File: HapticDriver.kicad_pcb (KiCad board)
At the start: 4 copper layers, 54.1 x 29 mm, 56 parts, among them J1 Conn_01x02_Pin, J10 Conn_01x02_Pin, J11 Conn_01x02_Pin, J12 Conn_01x02_Pin, J13 Conn_01x02_Pin, J14 USB_C_Receptacle_USB2.0, J2 Conn_01x02_Pin, J3 BATT PWR, J4 Conn_01x02_Pin, J5 Conn_01x02_Pin, J6 Conn_01x02_Pin, J7 Conn_01x02_Pin, J8 Conn_01x02_Pin, J9 Conn_01x02_Pin, SW1 BOOT, SW2 EN, U1 ESP32-S3-WROOM-2, U10 DRV8847SPWR, U11 REG1117-3.3, U2 DRV8847SPWR, U3 74HCT595, U4 74HCT595, U5 74HCT595, U6 DRV8847SPWR, U7 DRV8847SPWR, U8 DRV8847SPWR, U9 DRV8847SPWR

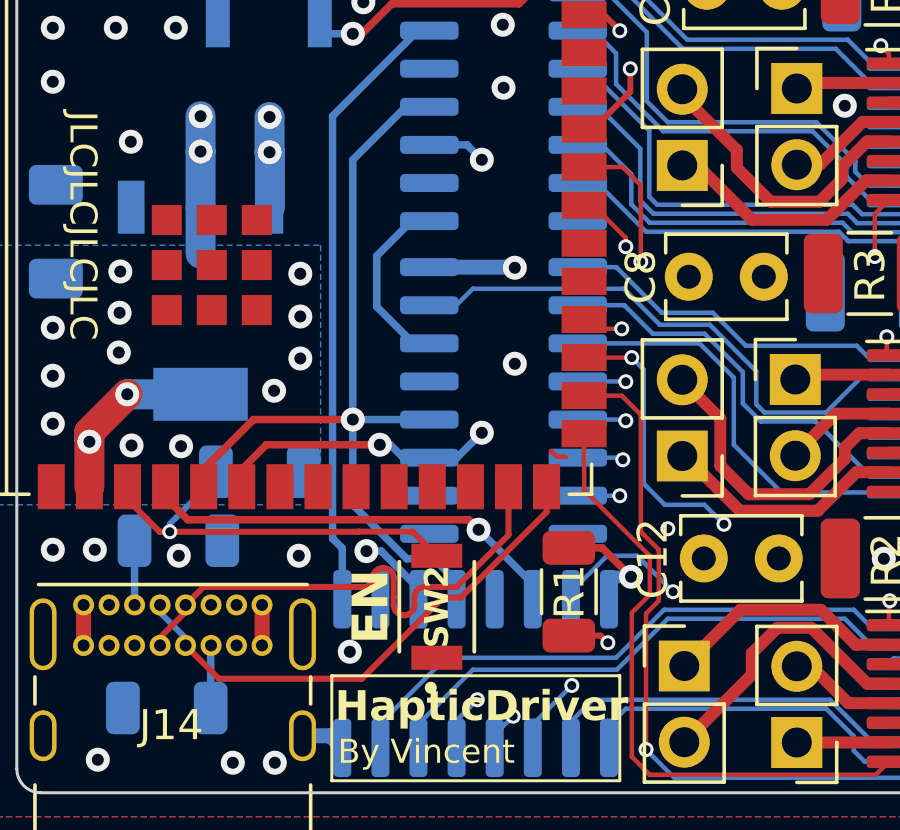
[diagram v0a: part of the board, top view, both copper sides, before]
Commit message: feat: pull OE and CLR shift reg pins to correct voltages
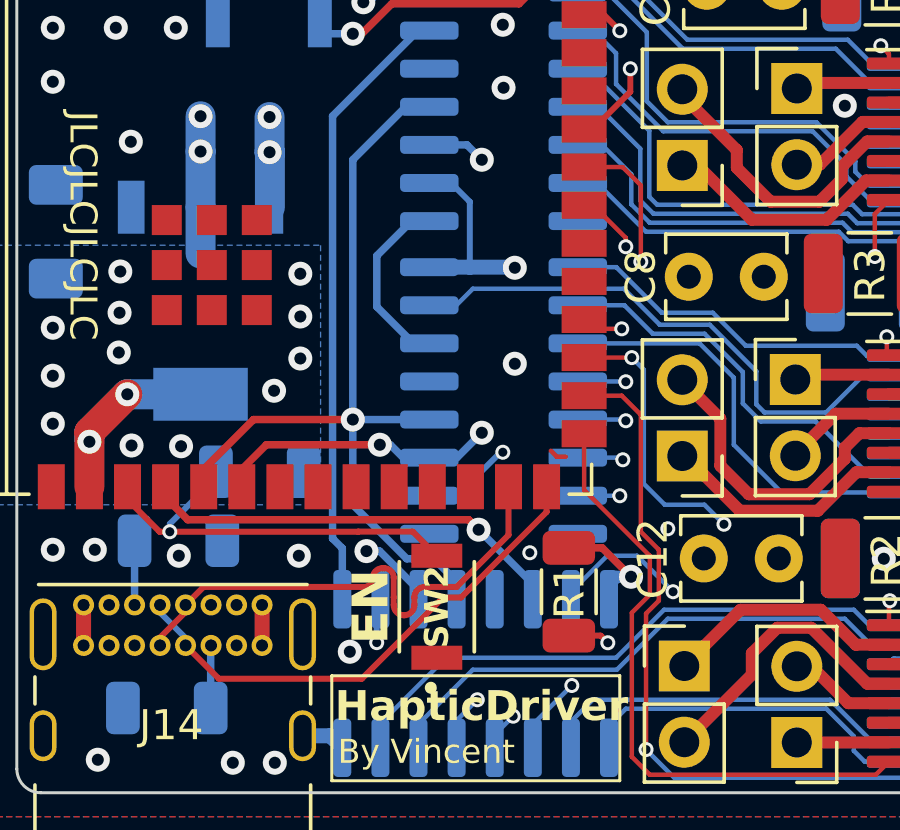
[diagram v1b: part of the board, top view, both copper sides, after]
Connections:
- U3 pad 10: unconnected-(U3-~{SRCLR}-Pad10) -> +3V3
- U3 pad 13: unconnected-(U3-~{OE}-Pad13) -> GND
- U4 pad 10: unconnected-(U4-~{SRCLR}-Pad10) -> +3V3
- U4 pad 13: unconnected-(U4-~{OE}-Pad13) -> GND
- U5 pad 10: unconnected-(U5-~{SRCLR}-Pad10) -> +3V3
- U5 pad 13: unconnected-(U5-~{OE}-Pad13) -> GND
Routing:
- net +3V3: track 72.2 -> 80.5 mm, vias 25 -> 27
- net GND: vias 34 -> 35

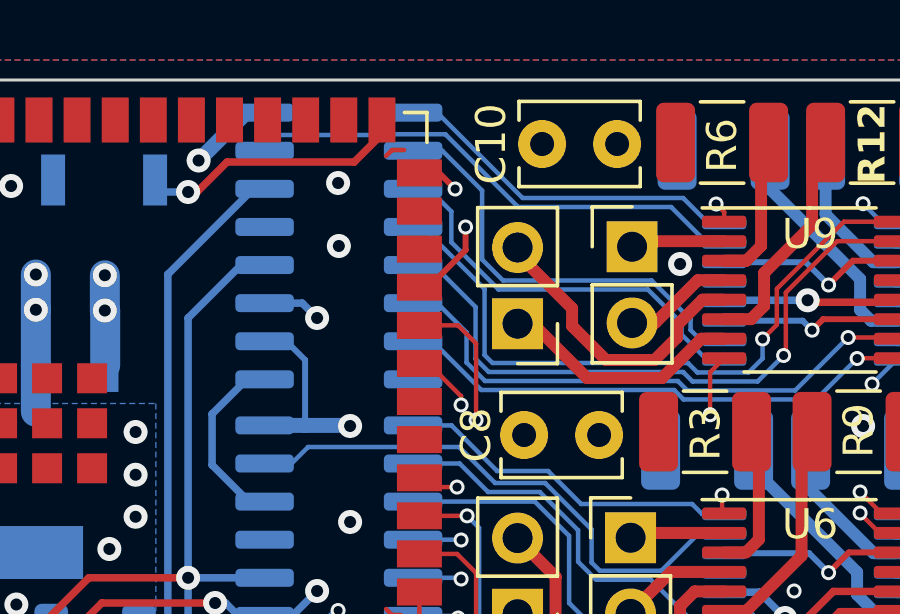
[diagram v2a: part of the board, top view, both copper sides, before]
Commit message: fix: avoid SDA on strapping pin GPIO45
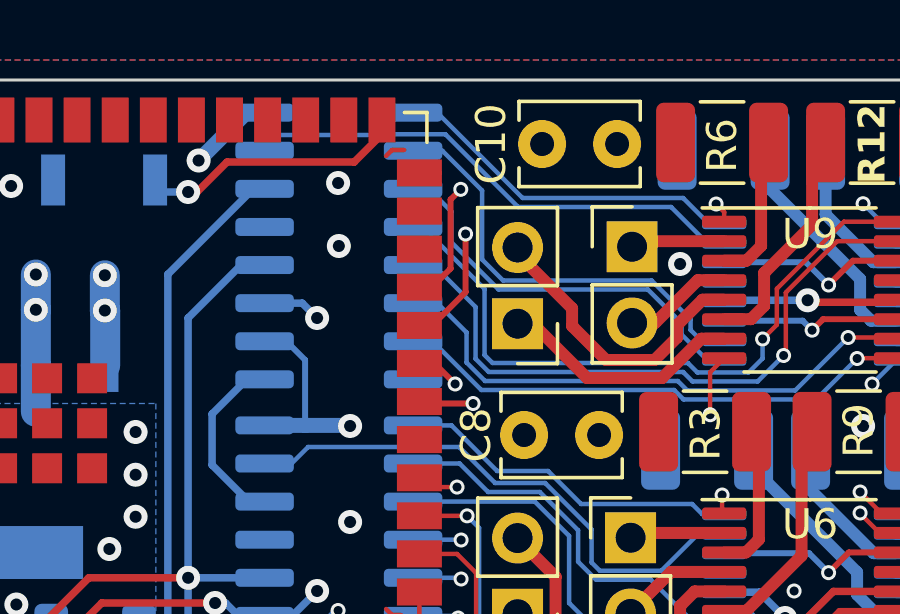
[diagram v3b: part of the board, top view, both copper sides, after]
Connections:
- U1 pad 20: unconnected-(U1-GPIO12/TOUCH12/ADC2_CH1/FSPICLK/FSPIIO6/SUBSPICLK-Pad20) -> /nFAULT_3
- U1 pad 22: /nFAULT_3 -> /DRV_SCL
- U1 pad 23: /DRV_SCL -> /DRV_SDA
- U1 pad 26: /DRV_SDA -> unconnected-(U1-GPIO45-Pad26)
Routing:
- net /nFAULT_3: track 20.2 -> 17.2 mm
- net /DRV_SDA: track 69.6 -> 72.0 mm
- net /DRV_SCL: track 53.1 -> 54.9 mm
- net unconnected-(U1-GPIO45-Pad26): track 0.00 -> 0.66 mm
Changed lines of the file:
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@@
 	(net 37 "/nFAULT_2")
 	(net 38 "unconnected-(U1-GPIO11{slash}TOUCH11{slash}ADC2_CH0{slash}FSPID{slash}FSPIIO5{slash}SUBSPID-Pad19)")
-	(net 39 "unconnected-(U1-GPIO12{slash}TOUCH12{slash}ADC2_CH1{slash}FSPICLK{slash}FSPIIO6{slash}SUBSPICLK-Pad20)")
+	(net 39 "unconnected-(U1-GPIO45-Pad26)")
 	(net 40 "/nFAULT_5")
 	(net 41 "/nFAULT_3")
@@
 			(size 1.5 0.9)
 			(layers "F.Cu" "F.Paste" "F.Mask")
-			(net 39 "unconnected-(U1-GPIO12{slash}TOUCH12{slash}ADC2_CH1{slash}FSPICLK{slash}FSPIIO6{slash}SUBSPICLK-Pad20)")
+			(net 41 "/nFAULT_3")
 			(pinfunction "GPIO12/TOUCH12/ADC2_CH1/FSPICLK/FSPIIO6/SUBSPICLK")
-			(pintype "bidirectional+no_connect")
+			(pintype "bidirectional")
 		)
 		(pad "21" smd rect
@@
 			(size 1.5 0.9)
 			(layers "F.Cu" "F.Paste" "F.Mask")
-			(net 41 "/nFAULT_3")
+			(net 63 "/DRV_SCL")
 			(pinfunction "GPIO14/TOUCH14/ADC2_CH3/FSPIWP/FSPIDQS/SUBSPIWP")
 			(pintype "bidirectional")
@@
 			(size 1.5 0.9)
 			(layers "F.Cu" "F.Paste" "F.Mask")
-			(net 63 "/DRV_SCL")
+			(net 27 "/DRV_SDA")
 			(pinfunction "GPIO21")
 			(pintype "bidirectional")
@@
 			(size 1.5 0.9)
 			(layers "F.Cu" "F.Paste" "F.Mask")
-			(net 27 "/DRV_SDA")
+			(net 39 "unconnected-(U1-GPIO45-Pad26)")
 			(pinfunction "GPIO45")
-			(pintype "bidirectional")
+			(pintype "bidirectional+no_connect")
 		)
 		(pad "27" smd rect
@@
 	)
 	(segment
-		(start 127.565 74.765)
-		(end 126.91 74.765)
-		(width 0.2)
-		(layer "F.Cu")
-		(net 27)
-	)
-	(segment
 		(start 141.053304 96.415)
 		(end 142.795 96.415)
@@
 	)
 	(segment
-		(start 128.1 75.3)
-		(end 127.565 74.765)
+		(start 127.9495 77.9505)
+		(end 127.325 78.575)
 		(width 0.2)
 		(layer "F.Cu")
@@
 	)
 	(segment
+		(start 127.325 78.575)
+		(end 126.91 78.575)
+		(width 0.2)
+		(layer "F.Cu")
+		(net 27)
+	)
+	(segment
+		(start 128.289124 75.310876)
+		(end 127.9495 75.6505)
+		(width 0.2)
+		(layer "F.Cu")
+		(net 27)
+	)
+	(segment
 		(start 140.5495 88.089503)
 		(end 141.224003 87.415)
@@
 		(net 27)
 	)
+	(segment
+		(start 127.9495 75.6505)
+		(end 127.9495 77.9505)
+		(width 0.2)
+		(layer "F.Cu")
+		(net 27)
+	)
 	(via
-		(at 128.1 75.3)
+		(at 128.289124 75.310876)
 		(size 0.5)
 		(drill 0.3)
@@
 	)
 	(segment
-		(start 128.1 75.3)
-		(end 137.3495 75.3)
+		(start 140.710919 97.967215)
+		(end 140.710919 96.757385)
 		(width 0.2)
 		(layer "In1.Cu")
@@
 	)
 	(segment
-		(start 140.710919 97.967215)
-		(end 140.710919 96.757385)
+		(start 128.3 75.3)
+		(end 137.3495 75.3)
 		(width 0.2)
 		(layer "In1.Cu")
@@
 	)
 	(segment
-		(start 137.3495 75.3)
-		(end 140.5495 78.5)
+		(start 128.289124 75.310876)
+		(end 128.3 75.3)
 		(width 0.2)
 		(layer "In1.Cu")
@@
 	)
 	(segment
+		(start 137.3495 75.3)
+		(end 140.5495 78.5)
+		(width 0.2)
+		(layer "In1.Cu")
+		(net 27)
+	)
+	(segment
 		(start 127.7 96.1)
 		(end 129.3 97.7)
@@
 	)
 	(segment
+		(start 127.565 74.765)
+		(end 126.91 74.765)
+		(width 0.2)
+		(layer "F.Cu")
+		(net 39)
+	)
+	(segment
 		(start 127.382356 81.115)
 		(end 126.91 81.115)
@@
 	)
 	(segment
-		(start 126.91 81.115)
-		(end 127.21 81.115)
-		(width 0.15)
+		(start 127.416706 81.115)
+		(end 126.91 81.115)
+		(width 0.2)
 		(layer "F.Cu")
 		(net 40)
 	)
 	(segment
-		(start 128.3 82.205)
-		(end 128.3 82.5)
-		(width 0.15)
+		(start 128.100853 81.799147)
+		(end 127.416706 81.115)
+		(width 0.2)
 		(layer "F.Cu")
 		(net 40)
 	)
 	(segment
-		(start 127.21 81.115)
-		(end 128.3 82.205)
+		(start 137.07 80.94)
+		(end 136.6 81.41)
 		(width 0.15)
 		(layer "F.Cu")
@@
 	)
 	(segment
-		(start 137.07 80.94)
-		(end 136.6 81.41)
+		(start 127.486982 81.115)
+		(end 126.91 81.115)
 		(width 0.15)
 		(layer "F.Cu")
@@
 	)
 	(via
-		(at 128.3 82.5)
+		(at 128.100853 81.799147)
 		(size 0.5)
 		(drill 0.3)
@@
 	)
 	(segment
-		(start 128.3 82.5)
-		(end 129 81.8)
+		(start 128.100853 81.799147)
+		(end 128.101706 81.8)
 		(width 0.15)
 		(layer "In2.Cu")
@@
 	)
 	(segment
-		(start 129 81.8)
+		(start 128.101706 81.8)
 		(end 135.575001 81.8)
 		(width 0.15)
@@
 	)
 	(segment
-		(start 128.8 80.450431)
-		(end 128.8 83)
-		(width 0.15)
-		(layer "F.Cu")
-		(net 41)
-	)
-	(segment
-		(start 128.194569 79.845)
-		(end 128.8 80.450431)
-		(width 0.15)
+		(start 128.7 82.450303)
+		(end 126.975303 82.450303)
+		(width 0.2)
 		(layer "F.Cu")
 		(net 41)
 	)
 	(segment
-		(start 126.91 79.845)
-		(end 128.194569 79.845)
-		(width 0.15)
+		(start 126.975303 82.450303)
+		(end 126.91 82.385)
+		(width 0.2)
 		(layer "F.Cu")
 		(net 41)
@@
 	)
 	(via
-		(at 128.8 83)
+		(at 128.7 82.450303)
 		(size 0.5)
 		(drill 0.3)
@@
 	)
 	(segment
-		(start 140.500001 83.299999)
-		(end 142 81.8)
-		(width 0.15)
-		(layer "In2.Cu")
-		(net 41)
-	)
-	(segment
-		(start 129.325 82.475)
-		(end 135.275 82.475)
+		(start 136.099999 83.299999)
+		(end 140.500001 83.299999)
 		(width 0.15)
 		(layer "In2.Cu")
@@
 	)
 	(segment
-		(start 136.099999 83.299999)
-		(end 140.500001 83.299999)
+		(start 128.7 82.450303)
+		(end 135.250303 82.450303)
 		(width 0.15)
 		(layer "In2.Cu")
@@
 	)
 	(segment
-		(start 135.275 82.475)
+		(start 135.250303 82.450303)
 		(end 136.099999 83.299999)
 		(width 0.15)
@@
 	)
 	(segment
-		(start 128.8 83)
-		(end 129.325 82.475)
+		(start 140.500001 83.299999)
+		(end 142 81.8)
 		(width 0.15)
 		(layer "In2.Cu")
@@
 	)
 	(segment
+		(start 126.91 79.845)
+		(end 127.545 79.845)
+		(width 0.15)
+		(layer "F.Cu")
+		(net 63)
+	)
+	(segment
 		(start 140 80.006547)
 		(end 140.366547 79.64)
@@
 	)
 	(segment
-		(start 128.4495 77.3355)
-		(end 127.21 78.575)
+		(start 128.4495 76.8)
+		(end 128.4495 78.7355)
 		(width 0.2)
 		(layer "F.Cu")
@@
 	)
 	(segment
-		(start 128.4495 76.566862)
-		(end 128.4495 77.3355)
+		(start 139.4 98.365)
+		(end 142.795 98.365)
 		(width 0.2)
 		(layer "F.Cu")
@@
 	)
 	(segment
-		(start 139.4 98.365)
-		(end 142.795 98.365)
+		(start 140.91 89.365)
+		(end 142.795 89.365)
 		(width 0.2)
 		(layer "F.Cu")
@@
 	)
 	(segment
-		(start 140.91 89.365)
-		(end 142.795 89.365)
+		(start 128.4495 78.7355)
+		(end 127.34 79.845)
 		(width 0.2)
 		(layer "F.Cu")
@@
 	)
 	(segment
-		(start 127.21 78.575)
-		(end 126.91 78.575)
+		(start 127.34 79.845)
+		(end 126.91 79.845)
 		(width 0.2)
 		(layer "F.Cu")
@@
 	)
 	(via
-		(at 128.4495 76.566862)
+		(at 128.4495 76.8)
 		(size 0.5)
 		(drill 0.3)
@@
 	)
 	(segment
-		(start 139.393395 98.358395)
-		(end 139.393395 97.006605)
+		(start 135.921519 76)
+		(end 139.928066 80.006547)
 		(width 0.2)
 		(layer "In1.Cu")
@@
 	)
 	(segment
-		(start 140 90.275)
-		(end 140 80.006547)
+		(start 139.393395 98.358395)
+		(end 139.393395 97.006605)
 		(width 0.2)
 		(layer "In1.Cu")
@@
 	)
 	(segment
-		(start 135.921519 76)
-		(end 139.928066 80.006547)
+		(start 139.928066 80.006547)
+		(end 140 80.006547)
 		(width 0.2)
 		(layer "In1.Cu")
@@
 	)
 	(segment
-		(start 139.928066 80.006547)
+		(start 140 90.275)
 		(end 140 80.006547)
 		(width 0.2)
@@
 	)
 	(segment
-		(start 128.4495 76.566862)
-		(end 129.016362 76)
+		(start 128.4495 76.8)
+		(end 129.2495 76)
 		(width 0.2)
 		(layer "In1.Cu")
@@
 	)
 	(segment
-		(start 140 96.4)
-		(end 140 90.275)
+		(start 129.2495 76)
+		(end 135.921519 76)
 		(width 0.2)
 		(layer "In1.Cu")
@@
 	)
 	(segment
-		(start 129.016362 76)
-		(end 135.921519 76)
+		(start 140 96.4)
+		(end 140 90.275)
 		(width 0.2)
 		(layer "In1.Cu")

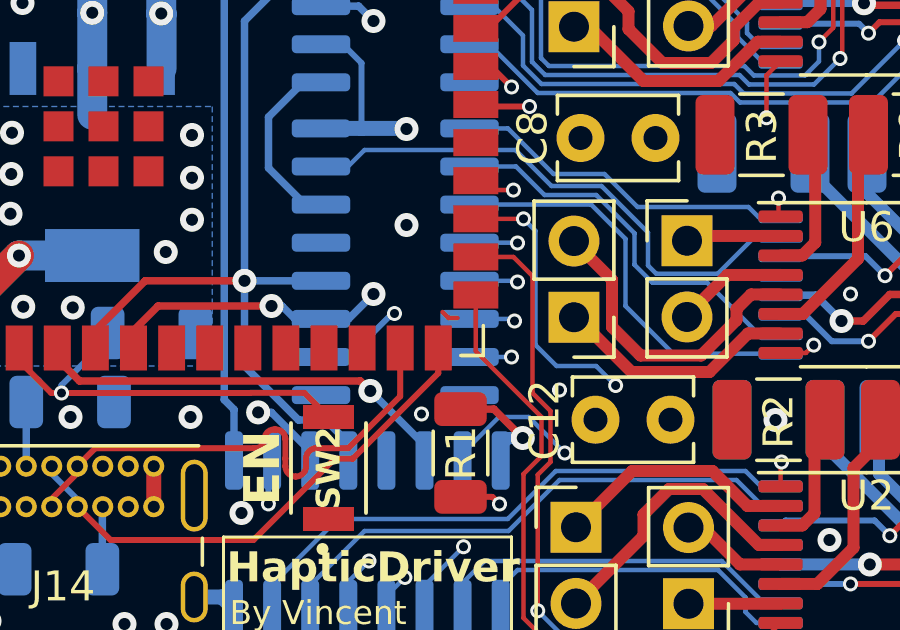
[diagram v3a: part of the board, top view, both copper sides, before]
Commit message: patch: specify value of sense resistor
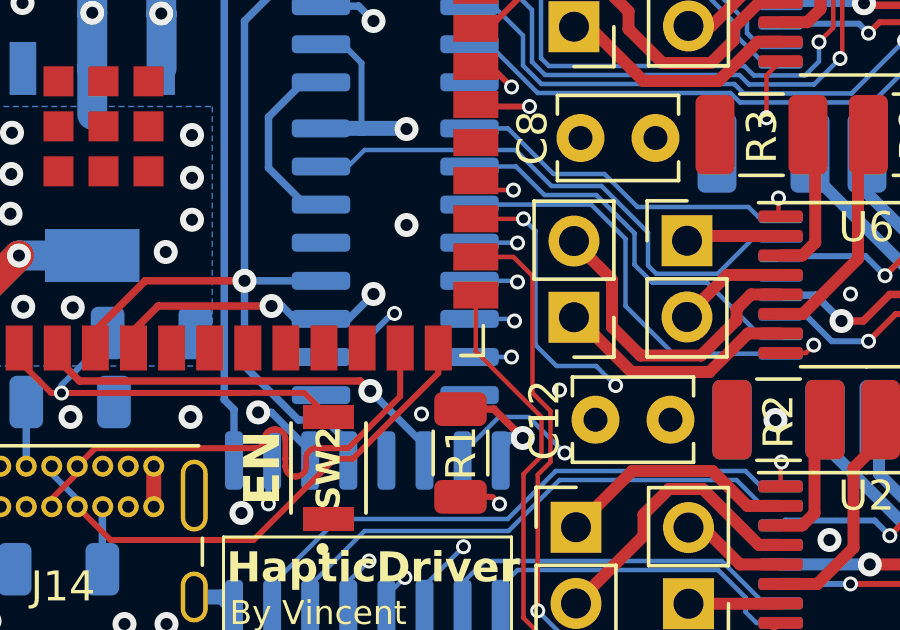
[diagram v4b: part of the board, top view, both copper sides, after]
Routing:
- net GND: track 5.46 -> 4.87 mm
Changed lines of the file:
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@@
-	)
-	(segment
-		(start 125.8 89.3)
-		(end 126 89.5)
-		(width 0.15)
-		(layer "F.Cu")
-		(net 2)
 	)
 	(segment
@@
 		(layer "F.Cu")
 		(net 2)
-	)
-	(segment
-		(start 126 89.5)
-		(end 126.3 89.5)
-		(width 0.15)
-		(layer "F.Cu")
-		(net 2)

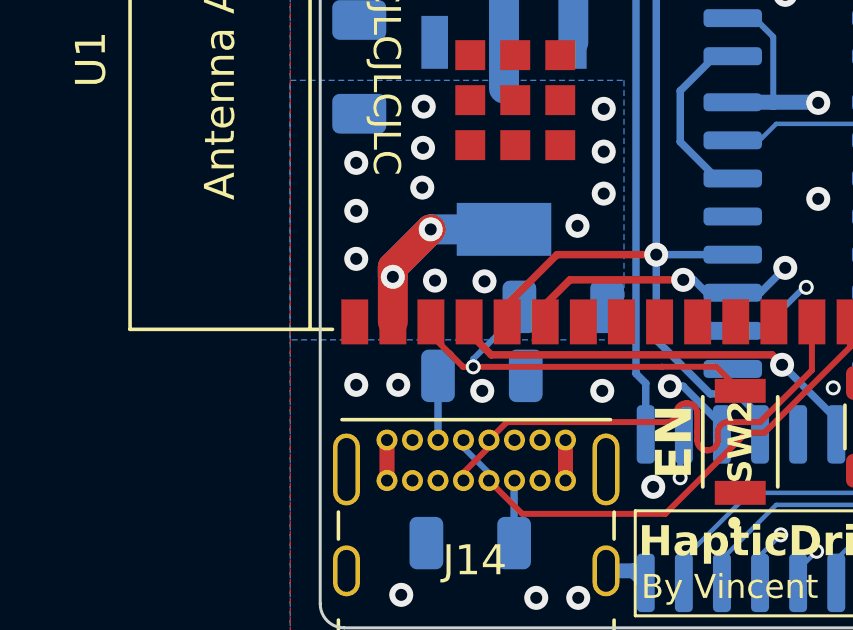
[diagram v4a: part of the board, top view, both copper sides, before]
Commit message: fix: delay rising of EN with cap, as per devkit design
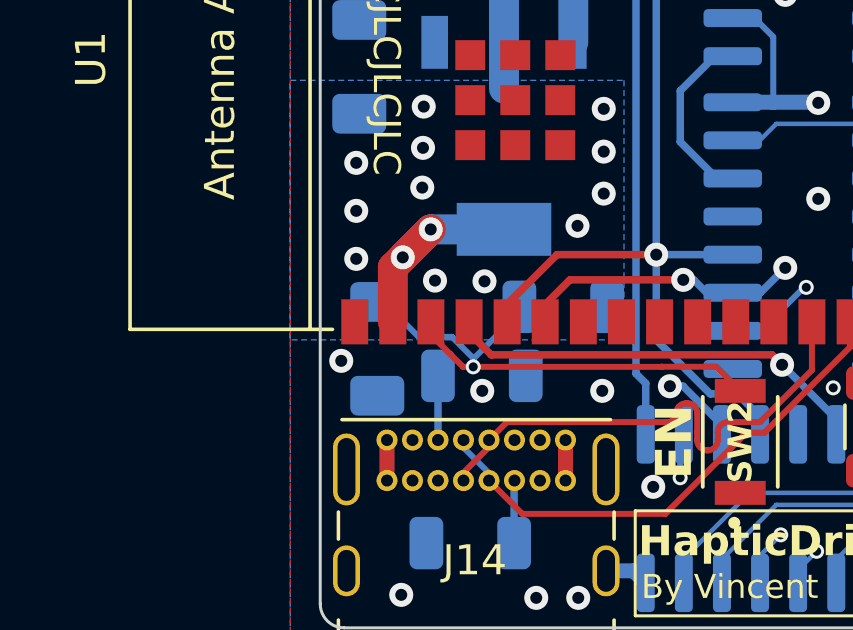
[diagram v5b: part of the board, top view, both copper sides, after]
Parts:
- added C14: 10uF, Capacitor_SMD:C_1206_3216Metric_Pad1.33x1.80mm_HandSolder, B.Cu at (109.9, 91.4)
- R10, R11, R12, R13, R2, R3, R4, R5, R6, R7, R8, R9: value R -> 150m
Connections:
- net Net-(U1-EN) renamed /EN
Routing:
- net /EN: track 14.2 -> 18.5 mm
- net +3V3: track 80.5 -> 79.7 mm
- net GND: vias 35 -> 34

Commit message: patch: improve silkscreen, add testpoints, optimise some traces
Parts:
- added TP1: TXD, TestPoint:TestPoint_Pad_1.5x1.5mm, B.Cu at (110.2, 73.1)
- added TP2: RXD, TestPoint:TestPoint_Pad_1.5x1.5mm, B.Cu at (112.7, 73.1)
- moved C3 5.50 mm to (158.0, 78.1)
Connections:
- U1 pad 36: unconnected-(U1-U0RXD/GPIO44/CLK_OUT2-Pad36) -> Net-(U1-U0RXD/GPIO44/CLK_OUT2)
- U1 pad 37: unconnected-(U1-U0TXD/GPIO43/CLK_OUT1-Pad37) -> Net-(U1-U0TXD/GPIO43/CLK_OUT1)
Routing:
- net Net-(U1-U0TXD/GPIO43/CLK_OUT1): track 0.00 -> 4.63 mm, vias 0 -> 1
- net Net-(U1-U0RXD/GPIO44/CLK_OUT2): track 0.00 -> 3.73 mm, vias 0 -> 1
- net GND: vias 34 -> 37
- net +3V3: vias 27 -> 30
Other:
- board text added: "MAX 15V"
- board text added: "USB Host"

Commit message: patch: final touch-ups, v0.1 fabrication
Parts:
- added C15: 10uF, Capacitor_SMD:C_1206_3216Metric_Pad1.33x1.80mm_HandSolder, F.Cu at (159.3, 83.2)
- moved C3 0.10 mm to (158.0, 78.0)
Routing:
- net +BATT: track 22.2 -> 23.4 mm, vias 5 -> 6
- net GND: vias 37 -> 42
